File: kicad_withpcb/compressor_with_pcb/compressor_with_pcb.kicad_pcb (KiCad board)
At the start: 2 copper layers, 128.3 x 105 mm, 135 parts, among them J1 EDA 306, J2 FRONT BOARD, Q1 BC549C, Q2 BC549C, Q3 BC549C, Q4 BC549C, Q5 BC549C, Q6 BC549C, Q7 BC549C, Q8 BC549C, Q9 BC549C, U1 NE5532, U2 NE5532, U3 NE5532, U4 TL072, U5 NE5532, U6 NE5532, U7 NE5532

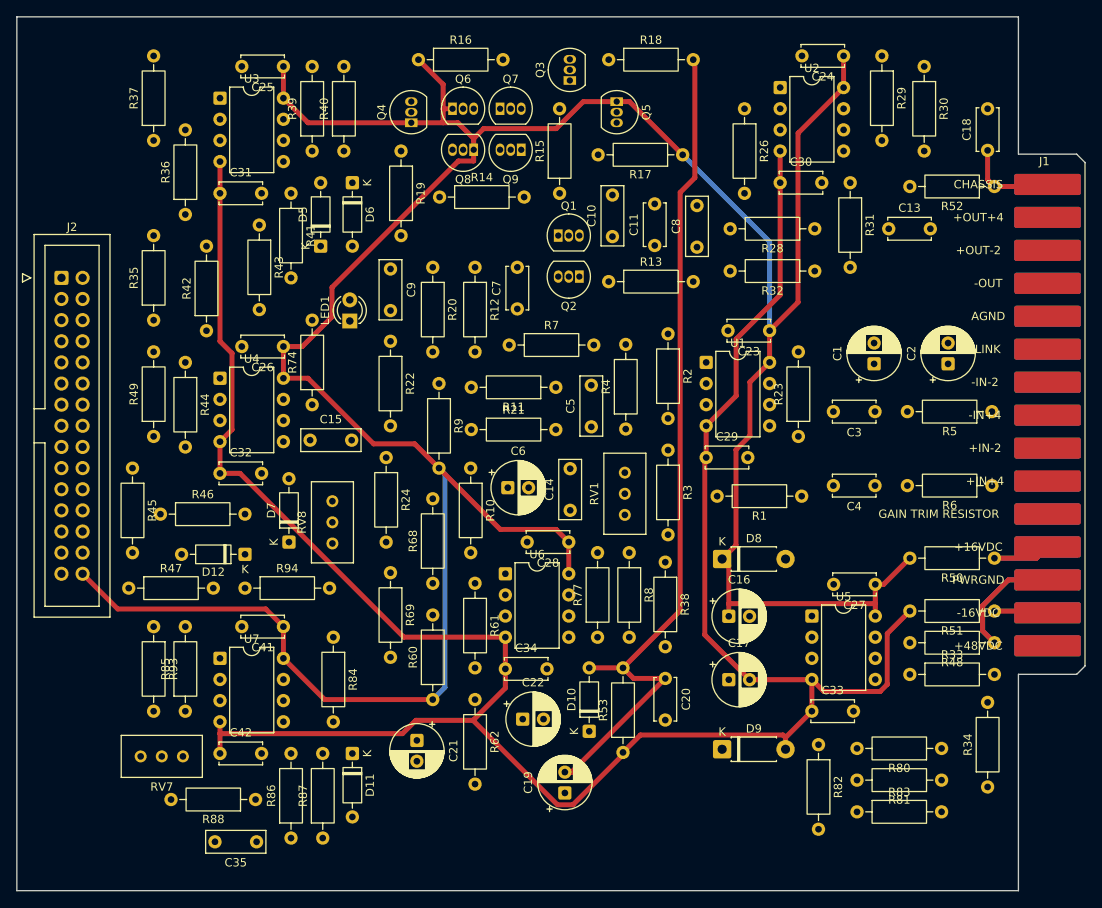
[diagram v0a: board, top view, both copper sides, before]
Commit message: Route the audio path
Balanced input and output, the input receiver and pad, the gain cell with
its recovery amp, makeup and output drivers, and the aux in and out. The
bypass lines run forward to J2 for the switch on the front board.

Co-Authored-By: Claude Opus 5.5 (1M context) <noreply@anthropic.com>
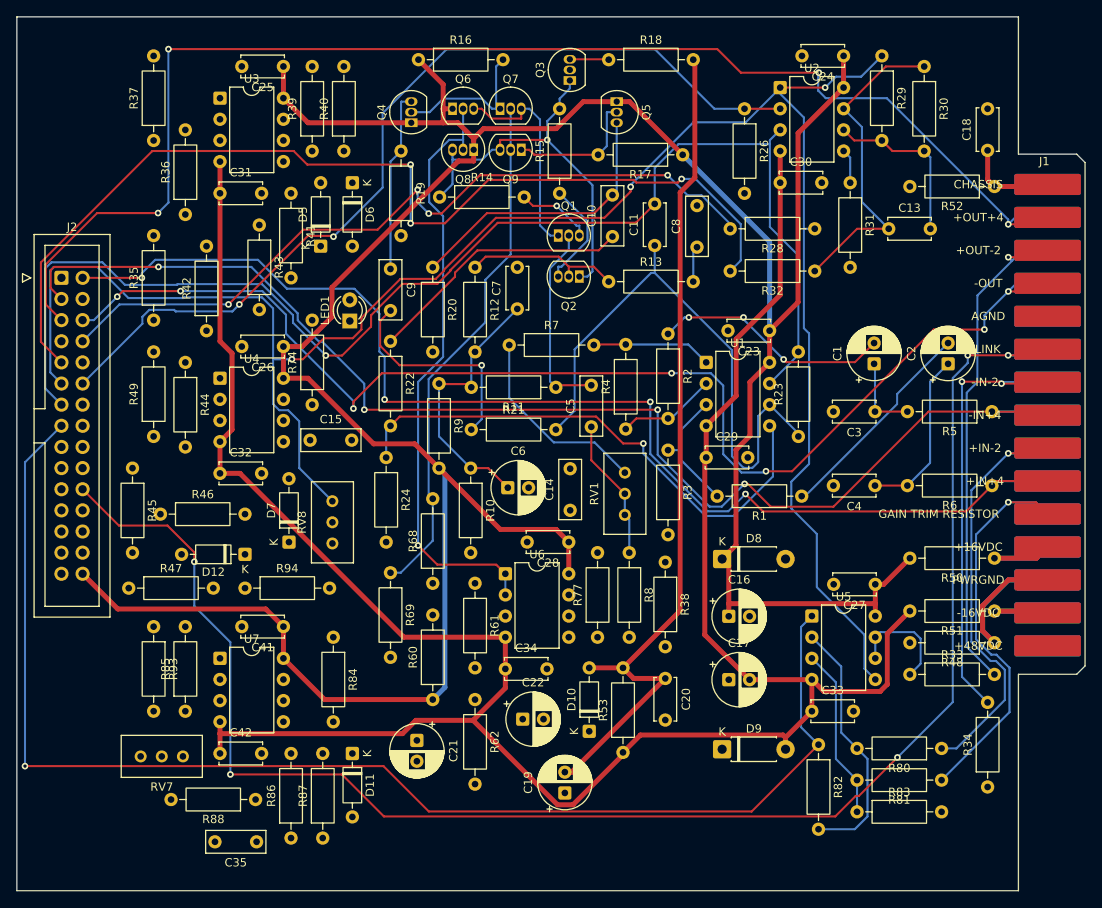
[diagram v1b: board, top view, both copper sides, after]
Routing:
- net OUT-A: track 0.00 -> 238.2 mm, vias 0 -> 3
- net LINK: track 0.00 -> 197.0 mm, vias 0 -> 5
- net OUT+: track 0.00 -> 165.2 mm, vias 0 -> 4
- net KEY: track 0.00 -> 160.5 mm, vias 0 -> 1
- net SIG-VCA: track 0.00 -> 157.5 mm, vias 0 -> 1
- net IN-: track 0.00 -> 155.4 mm, vias 0 -> 4
- net OUT-: track 0.00 -> 152.7 mm, vias 0 -> 7
- net IN+: track 0.00 -> 149.2 mm, vias 0 -> 4
- net BYP_B: track 0.00 -> 121.3 mm, vias 0 -> 3
- net MAKEUP_FB: track 0.00 -> 109.4 mm, vias 0 -> 2
- net BYP_A: track 0.00 -> 92.4 mm, vias 0 -> 4
- net STA: track 0.00 -> 72.7 mm, vias 0 -> 1
- net Net-(U1B--): track 0.00 -> 69.9 mm
- net Net-(U1B-+): track 0.00 -> 64.3 mm, vias 0 -> 1
- net AUXOUT+: track 0.00 -> 63.8 mm, vias 0 -> 1
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
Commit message: Route the sidechain and meter lines
Detector, threshold, ratio and timing, the steering reference, and the two
meter feeds, with the long slow runs going forward to J2.

Co-Authored-By: Claude Opus 5.5 (1M context) <noreply@anthropic.com>
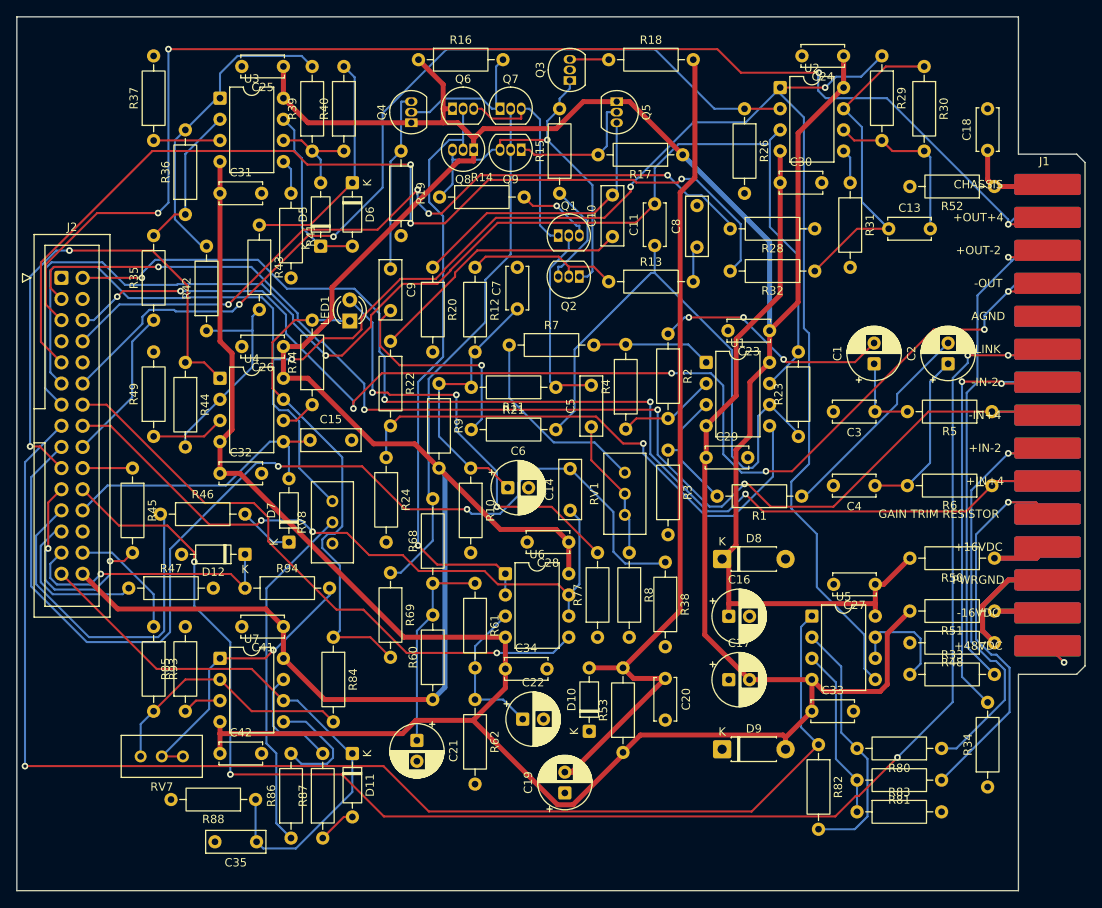
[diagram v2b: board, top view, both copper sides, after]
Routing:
- net HPF_B: track 0.00 -> 125.2 mm, vias 0 -> 2
- net HPF_A: track 0.00 -> 80.9 mm, vias 0 -> 2
- net KEY_SRC: track 0.00 -> 73.3 mm, vias 0 -> 1
- net LVL_METER: track 0.00 -> 68.3 mm
- net RATIO_CW: track 0.00 -> 61.5 mm, vias 0 -> 2
- net CTRL-B: track 0.00 -> 60.0 mm
- net Net-(LED1-A): track 0.00 -> 52.3 mm, vias 0 -> 3
- net ATK_W: track 0.00 -> 42.7 mm
- net Net-(R86-Pad1): track 0.00 -> 42.5 mm
- net Net-(R36-Pad2): track 0.00 -> 37.6 mm
- net TIMING: track 0.00 -> 35.6 mm
- net Net-(R94-Pad2): track 0.00 -> 34.4 mm, vias 0 -> 1
- net GR_METER: track 0.00 -> 32.6 mm, vias 0 -> 1
- net Net-(U7A--): track 0.00 -> 31.4 mm
- net Net-(D6-K): track 0.00 -> 27.9 mm
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
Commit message: Pour AGND on the bottom layer
Every AGND pad is tied in with a thin track first, so nothing depends on a
sliver of pour, then the bottom layer is poured with thermal reliefs. Three
pads that only touched a stray island are taken off the pour and rely on
their track.

Co-Authored-By: Claude Opus 5.5 (1M context) <noreply@anthropic.com>
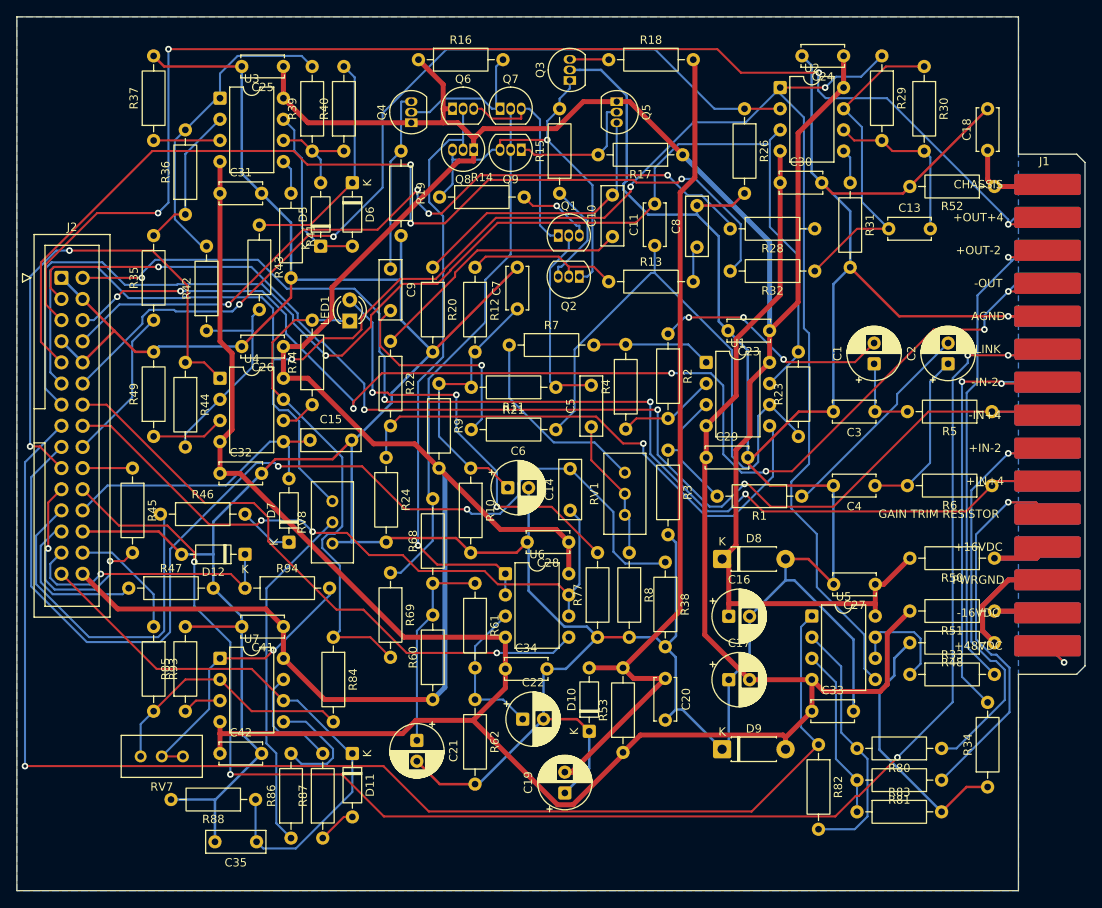
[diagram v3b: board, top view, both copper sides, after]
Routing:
- net AGND: track 0.00 -> 678.7 mm, vias 0 -> 1
- added copper zone on B.Cu, net AGND

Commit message: Clear DRC on the main board
- Reference designators sit inside their own outlines, or beside the small
  parts, so none overlap a neighbour or a pad
- Edge finger pads open the mask on their own side only
- A board rule allows the TO-92 footprint's own 0.22 mm pad gap, which the
  Power and Ground classes would otherwise flag
- J1 pin labels move to the fab layer, they ran under parts by the fingers
- Board name and revision on the silkscreen

DRC: 0 errors, 0 unconnected, schematic parity clean. Two warnings remain,
the template's missing Cards library and one K mark touching R41's outline.

Co-Authored-By: Claude Opus 5.5 (1M context) <noreply@anthropic.com>
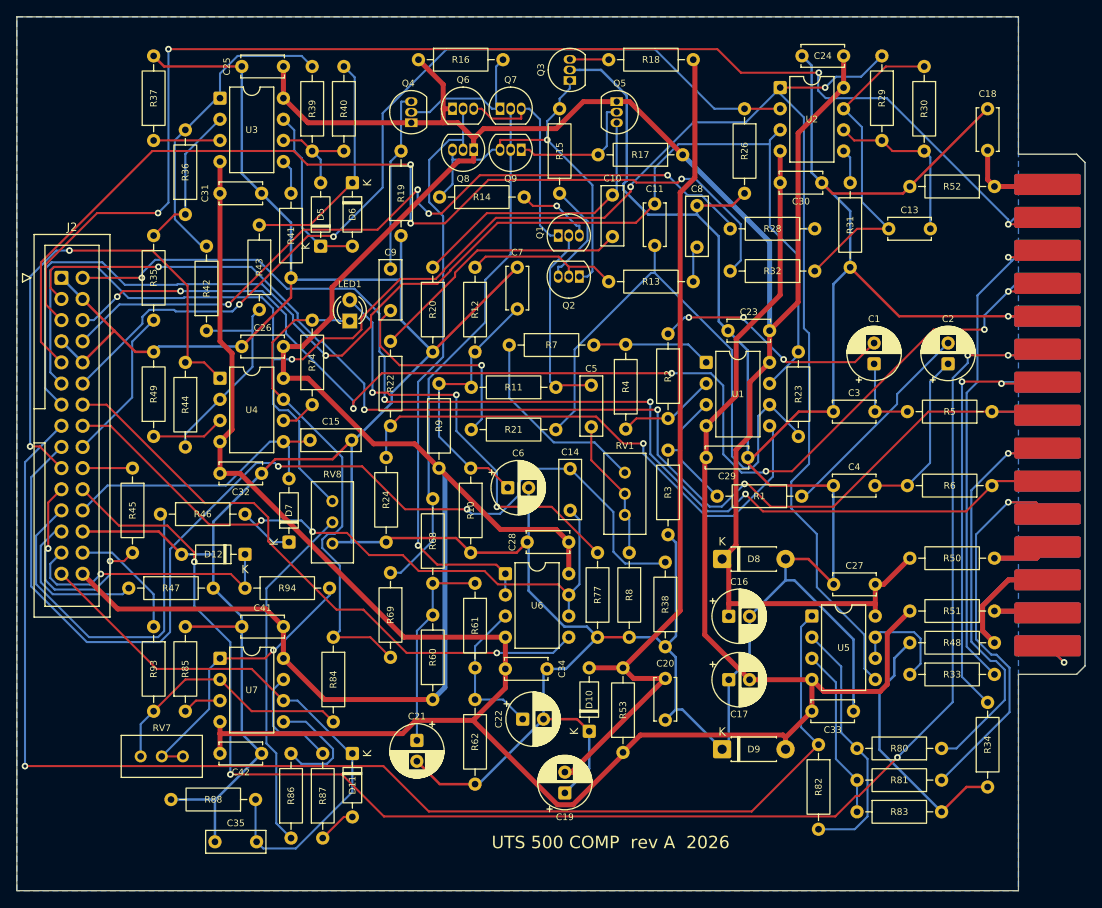
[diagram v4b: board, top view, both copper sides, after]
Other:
- board text added: "UTS 500 COMP rev A 2026"

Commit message: Put the op amps in sockets
U1 to U7 use the DIP-8 socket footprint. The pads are the same, so the
routing and pour are untouched; only the outlines grow. References moved back
inside them.

DRC unchanged: 0 errors, 0 unconnected, parity clean.

Co-Authored-By: Claude Opus 5.5 (1M context) <noreply@anthropic.com>
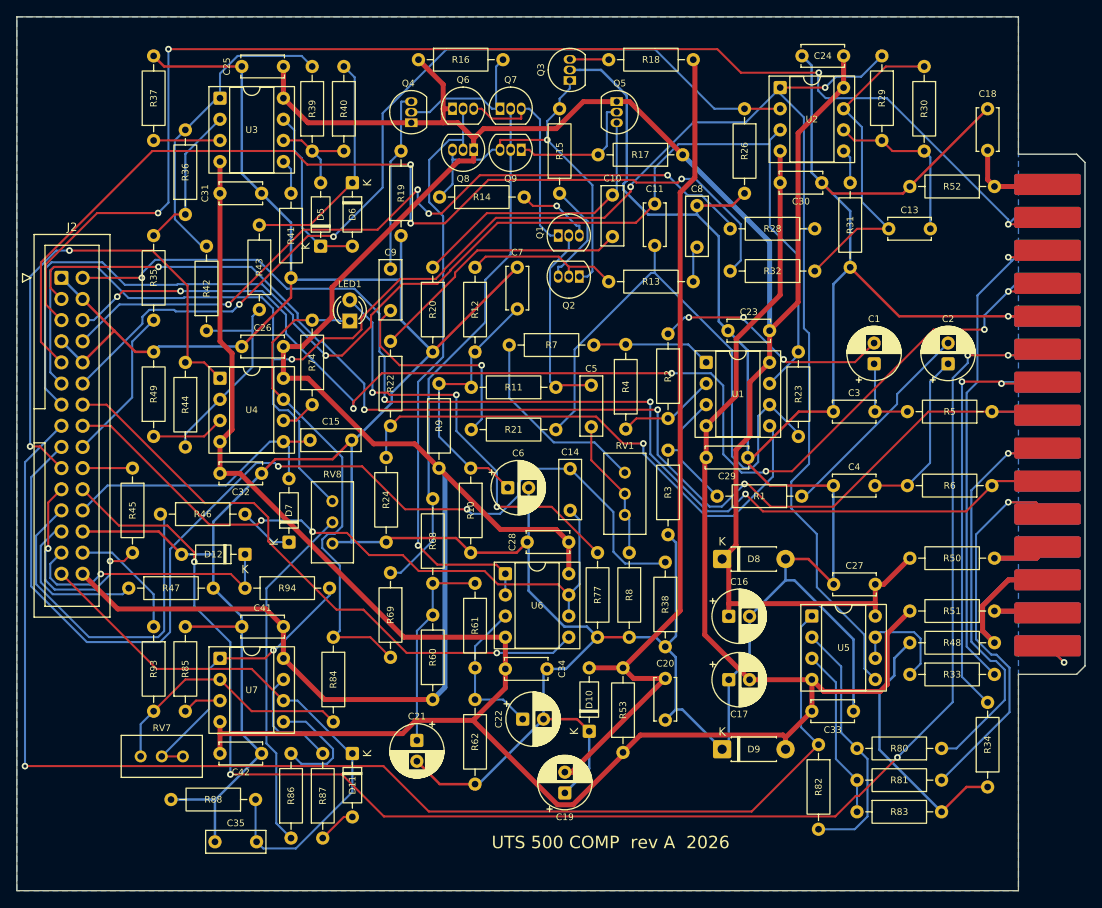
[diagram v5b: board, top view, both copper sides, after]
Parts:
- U1, U2, U3, U4, U5, U6, U7: footprint Package_DIP:DIP-8_W7.62mm -> Package_DIP:DIP-8_W7.62mm_Socket

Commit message: Add bracket holes to the main board and document the joint
Two M3 holes by the front edge, 82 mm apart, for the L-bracket to the
panel. H2 is plated and routed to CHASSIS so the bracket grounds the panel;
H1 is unplated. README now covers the ribbon, its length and orientation,
and how each board fixes to the faceplate.

DRC unchanged: 0 errors, 0 unconnected, parity clean.

Co-Authored-By: Claude Opus 5.5 (1M context) <noreply@anthropic.com>
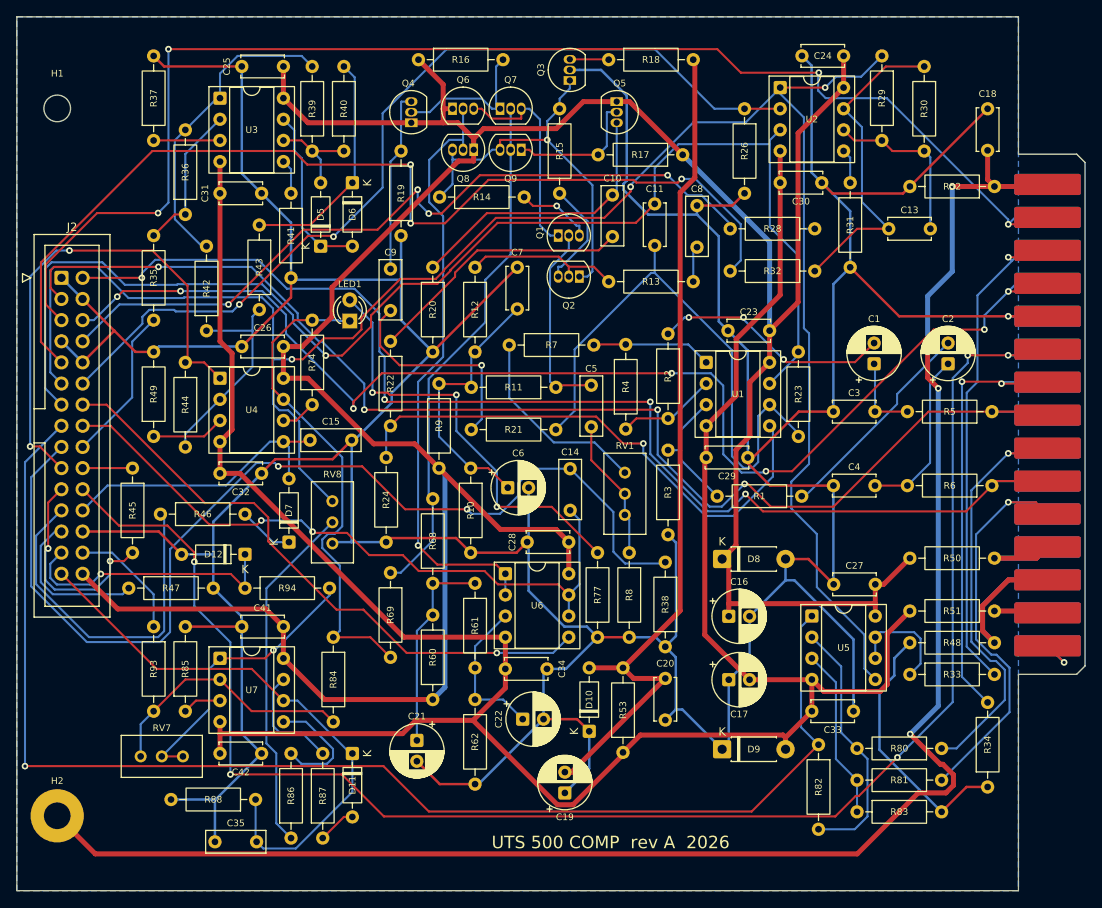
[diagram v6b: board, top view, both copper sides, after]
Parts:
- added H1: Bracket M3, MountingHole:MountingHole_3.2mm_M3, F.Cu at (79.5, 66.0)
- added H2: Bracket M3, MountingHole:MountingHole_3.2mm_M3_Pad, F.Cu at (79.5, 151.0)
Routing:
- net CHASSIS: track 17.7 -> 213.2 mm, vias 0 -> 4
